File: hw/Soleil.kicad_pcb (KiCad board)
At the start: 2 copper layers, 31.4 x 44 mm, 54 parts, among them J1 Conn_01x04, Q1 MMBT3904, Q2 Si2301, Q3 2N7002, SW1 SW_Push, U1 SPV1040TTR, U2 XS3A1T3157GMX, U3 TPS61220DCK, U4 STM32G030F6Px, U5 ZJY200200-0154DAAMFGN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

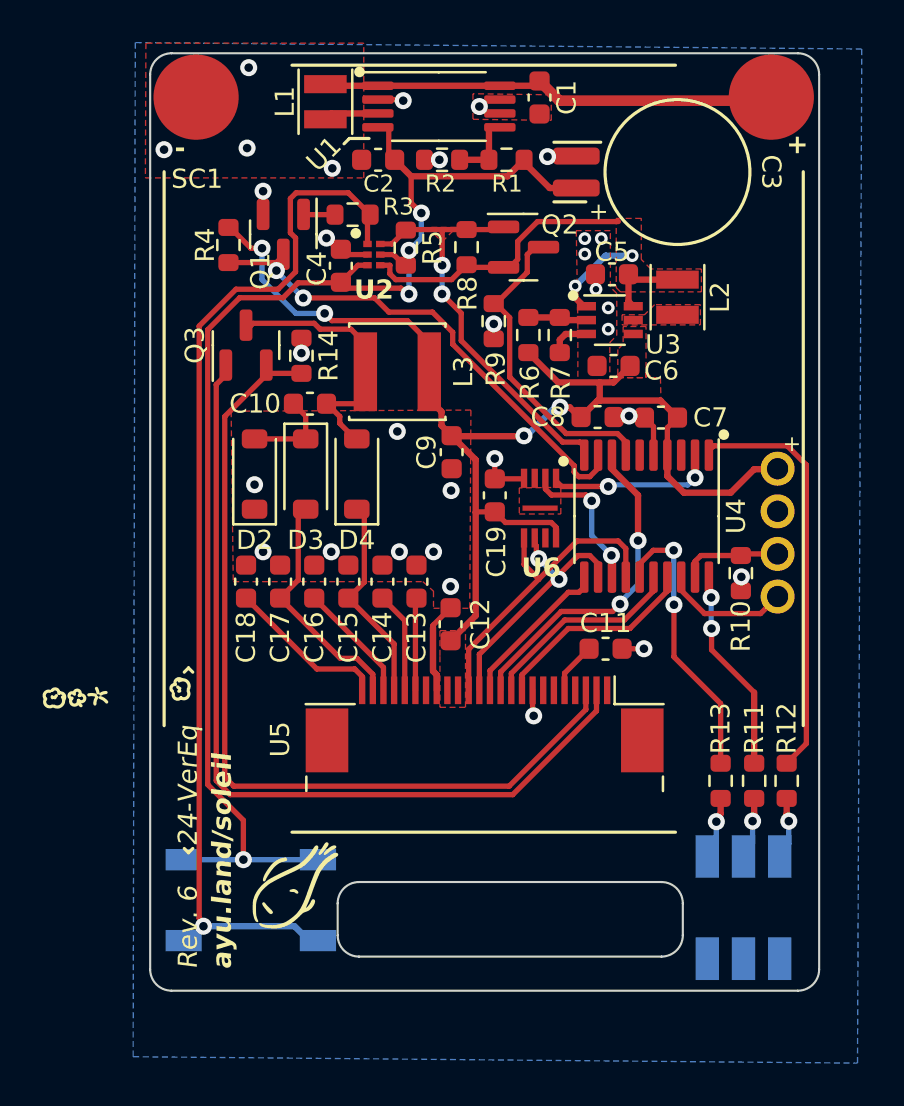
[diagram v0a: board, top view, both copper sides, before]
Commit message: Revise hardware and submit for fabrication (Rev. 6)
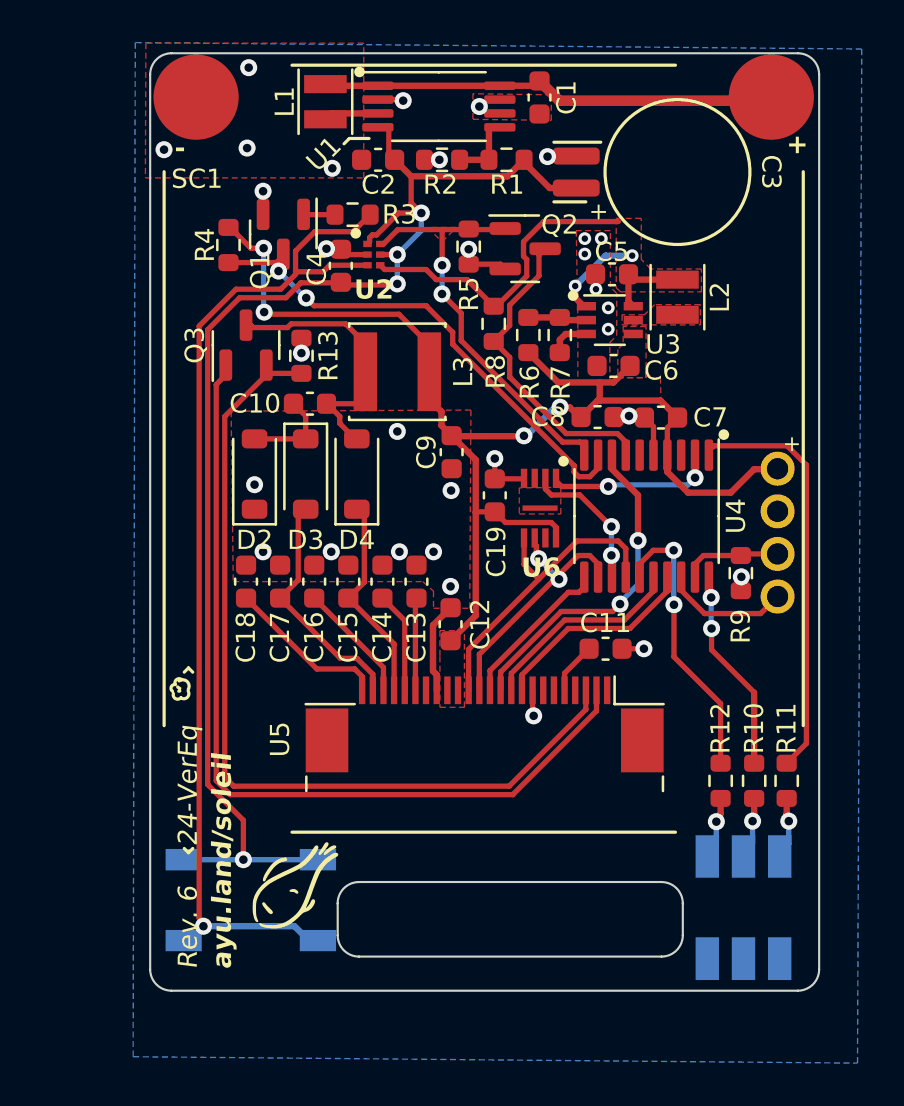
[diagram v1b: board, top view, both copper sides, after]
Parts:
- removed the R8 at (20.9, 18.5)
- Q2: value Si2301 -> 2N7002
- moved R5 2.95 mm to (21.1, 18.5), turned to -90 degrees
- moved R8 0.12 mm to (22.2, 22.1)
- moved Q2 0.11 mm to (23.7, 18.6)
- renumbered R11 to R10, R12 to R11, R13 to R12, R14 to R13, R9 to R8, R10 to R9
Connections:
- Q2 pad 2: VRI -> GND
- R3 pad 2: Net-(U2-Y2) -> Net-(U2-Y1)
- R5 pad 1: VCAP -> PWR_LATCH
- R5 pad 2: PWR_LATCH -> GND
- R8 pad 1: VRI_SENSE -> VRI
- R8 pad 2: GND -> VRI_SENSE
- SW1 pad 2: Net-(U2-Y2) -> Net-(U2-Y1)
- U2 pad 1: Net-(U2-Y2) -> VCAP
- U2 pad 3: VCAP -> Net-(U2-Y1)
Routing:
- net Net-(U2-Y2): track 49.6 -> 0.00 mm, vias 1 -> 0
- net Net-(U2-Y1): track 0.00 -> 49.1 mm, vias 0 -> 1
- net GND: track 21.5 -> 23.1 mm
- net VRI: track 21.9 -> 23.3 mm
- net VDD: track 60.6 -> 61.3 mm
- net VCAP: track 64.1 -> 63.5 mm

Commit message: Update layout, 🚧 routing to-do
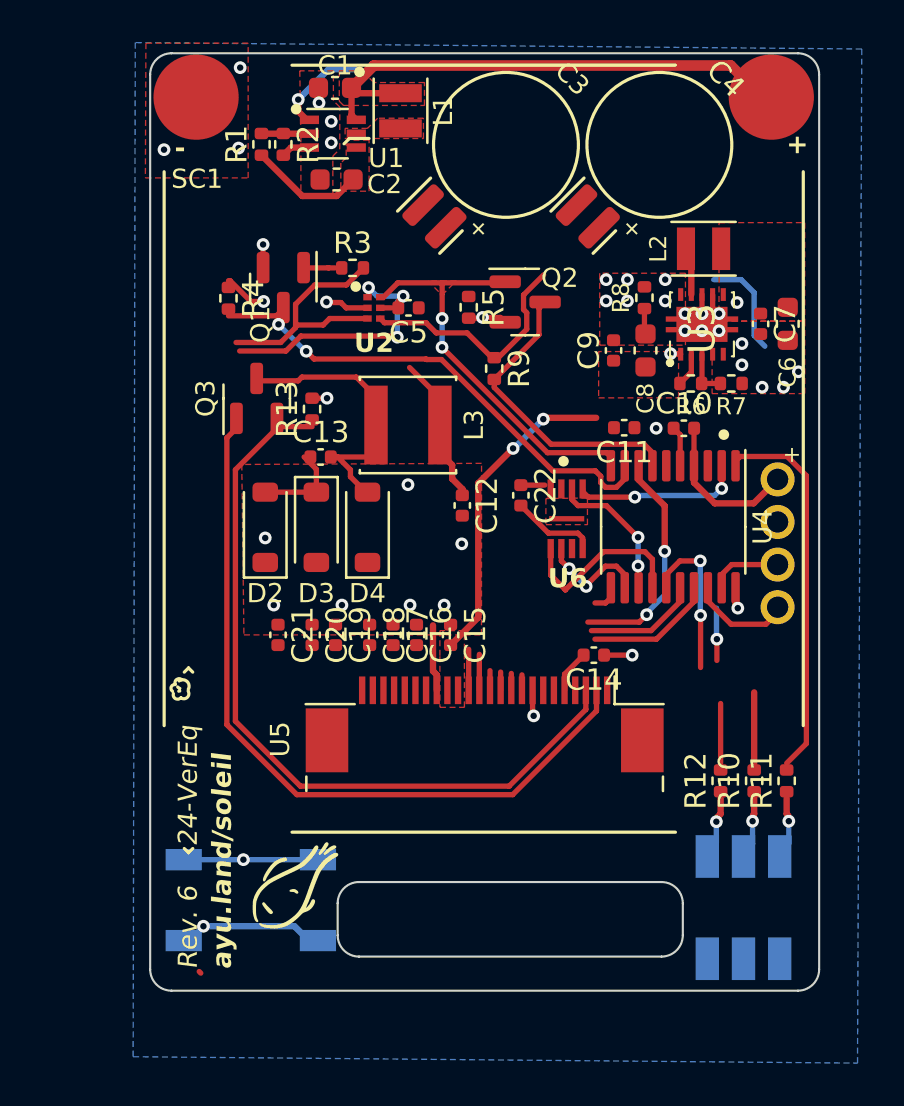
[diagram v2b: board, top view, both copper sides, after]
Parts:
- removed the C1 at (24.4, 11.5)
- removed the C2 at (16.8, 14.4)
- removed the L1 at (14.3, 11.7)
- removed the R1 at (22.8, 14.4)
- removed the R2 at (19.8, 14.4)
- removed the R9 at (33.8, 33.8)
- removed the U1 at (19.6, 11.9)
- added C4: 220m, Soleil_footprints:DMS3R3, F.Cu at (30.0, 13.7)
- added C6: 10u, Capacitor_SMD:C_0603_1608Metric, F.Cu at (36.0, 22.1)
- added C7: 100n, Capacitor_SMD:C_0402_1005Metric, F.Cu at (34.8, 22.1)
- added C8: 10u, Capacitor_SMD:C_0603_1608Metric, F.Cu at (29.4, 23.4)
- added C9: 2.2u, Capacitor_SMD:C_0402_1005Metric, F.Cu at (27.9, 23.4)
- added L2: 10u, Inductor_SMD:L_Sunlord_SWPA252012S, F.Cu at (32.1, 18.6)
- added R6: 560k, Resistor_SMD:R_0402_1005Metric, F.Cu at (31.5, 24.9)
- added R7: 100k, Resistor_SMD:R_0402_1005Metric, F.Cu at (33.4, 24.9)
- added R8: 1, Resistor_SMD:R_0402_1005Metric, F.Cu at (29.3, 20.9)
- added U3: TPS61020DRCR, Soleil_footprints:TPS61020DRCR, F.Cu at (32.0, 22.1)
- C10: renamed from C7; footprint Capacitor_SMD:C_0603_1608Metric -> Capacitor_SMD:C_0402_1005Metric
- C11: renamed from C8; footprint Capacitor_SMD:C_0603_1608Metric -> Capacitor_SMD:C_0402_1005Metric
- C12: renamed from C9; footprint Capacitor_SMD:C_0603_1608Metric -> Capacitor_SMD:C_0402_1005Metric
- C13: renamed from C10; footprint Capacitor_SMD:C_0603_1608Metric -> Capacitor_SMD:C_0402_1005Metric
- C14: renamed from C11; footprint Capacitor_SMD:C_0603_1608Metric -> Capacitor_SMD:C_0402_1005Metric
- C15: renamed from C12; footprint Capacitor_SMD:C_0603_1608Metric -> Capacitor_SMD:C_0402_1005Metric
- C16: renamed from C13; footprint Capacitor_SMD:C_0603_1608Metric -> Capacitor_SMD:C_0402_1005Metric
- C17: renamed from C14; footprint Capacitor_SMD:C_0603_1608Metric -> Capacitor_SMD:C_0402_1005Metric
- C18: renamed from C15; footprint Capacitor_SMD:C_0603_1608Metric -> Capacitor_SMD:C_0402_1005Metric
- C19: renamed from C16; footprint Capacitor_SMD:C_0603_1608Metric -> Capacitor_SMD:C_0402_1005Metric
- C20: renamed from C17; footprint Capacitor_SMD:C_0603_1608Metric -> Capacitor_SMD:C_0402_1005Metric
- C21: renamed from C18; footprint Capacitor_SMD:C_0603_1608Metric -> Capacitor_SMD:C_0402_1005Metric
- C22: renamed from C19; footprint Capacitor_SMD:C_0603_1608Metric -> Capacitor_SMD:C_0402_1005Metric
- C5: renamed from C4; footprint Capacitor_SMD:C_0603_1608Metric -> Capacitor_SMD:C_0402_1005Metric
- R1: renamed from R6; footprint Resistor_SMD:R_0603_1608Metric -> Resistor_SMD:R_0402_1005Metric
- R10, R11, R12, R13, R3, R4, R5: footprint Resistor_SMD:R_0603_1608Metric -> Resistor_SMD:R_0402_1005Metric
- R2: renamed from R7; footprint Resistor_SMD:R_0603_1608Metric -> Resistor_SMD:R_0402_1005Metric
- R9: renamed from R8; footprint Resistor_SMD:R_0603_1608Metric -> Resistor_SMD:R_0402_1005Metric
- moved R2 15.8 mm to (12.3, 13.7)
- moved C2 15.7 mm to (14.8, 15.3)
- moved L1 15.7 mm to (17.9, 12.1)
- moved U1 15.7 mm to (14.7, 13.2)
- moved C1 15.7 mm to (14.8, 11.0)
- moved R1 15.4 mm to (11.3, 13.7)
- moved C3 8.15 mm to (22.8, 13.7), turned to -135 degrees
- moved C5 3.74 mm to (18.2, 21.4), turned to 180 degrees
- moved C20 2.92 mm to (13.7, 36.7)
- moved C21 2.92 mm to (12.1, 36.7)
- moved R5 2.85 mm to (21.1, 21.3)
- moved C19 2.69 mm to (14.8, 36.7)
- moved C18 2.69 mm to (16.4, 36.7)
- moved C12 2.55 mm to (20.8, 30.6)
- moved C13 2.55 mm to (14.1, 28.4)
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- renumbered C5 to C1, C6 to C2, L2 to L1, U3 to U1
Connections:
- C1 pad 1: VRI -> Net-(SC1-+)
- C2 pad 1: VDD -> VCAP
- L1 pad 1: VRI -> Net-(SC1-+)
- R1 pad 1: VDD -> VCAP
- U1 pad 1: VRI -> Net-(SC1-+)
- U1 pad 4: VDD -> VCAP
- U1 pad 6: VRI -> Net-(SC1-+)
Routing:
- net VCAP: track 63.5 -> 24.9 mm
- net Net-(U2-Y1): track 49.1 -> 18.5 mm
- net VDD: track 61.3 -> 37.4 mm, vias 4 -> 3
- net VRI: track 23.3 -> 11.7 mm
- net EP_VGL: track 11.3 -> 0.00 mm
- net EP_VGH: track 9.92 -> 0.00 mm
- net Net-(U5-VCOM): track 7.62 -> 0.00 mm
- net Net-(SC1-+): track 21.7 -> 29.3 mm, vias 0 -> 1
- net Net-(U5-VSL): track 5.75 -> 0.00 mm
- net SPI_SCK: track 12.4 -> 6.96 mm
- net EP_CSN: track 7.44 -> 2.24 mm
- net EP_GDR: track 40.4 -> 35.4 mm
- net Net-(U5-VSH1): track 4.76 -> 0.00 mm
- net Net-(U5-VDD): track 4.70 -> 0.00 mm
- net SPI_MOSI: track 15.1 -> 10.5 mm
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- added copper zone on F.Cu, net Net-(SC1-+)
- added copper zone on F.Cu, net VCAP

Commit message: Finish board routing
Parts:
- C1, C2, C6, C8: footprint Capacitor_SMD:C_0603_1608Metric -> Capacitor_SMD:C_0402_1005Metric
- R3: value 470k -> 1M
- R4: value 470k -> 100k
- R6: value 560k -> 1M
- R7: value 100k -> 200k
- moved R3 0.74 mm to (15.1, 20.0), turned to -90 degrees
- moved R4 0.53 mm to (10.1, 21.3)
- moved C12 0.52 mm to (20.8, 30.1)
- moved C2 0.47 mm to (14.8, 14.8)
- moved R8 0.43 mm to (29.7, 20.9)
- moved C7 0.42 mm to (35.2, 22.1)
- moved C8 0.42 mm to (29.8, 23.4)
- moved C9 0.42 mm to (28.3, 23.4)
- moved L2 0.42 mm to (32.5, 18.6)
- moved R6 0.42 mm to (31.9, 24.9)
- moved R7 0.42 mm to (33.8, 24.9)
- moved U3 0.42 mm to (32.4, 22.1)
- moved C1 0.33 mm to (15.1, 10.9)
- moved C22 0.30 mm to (23.8, 30.1)
- moved L1 0.25 mm to (17.9, 11.8)
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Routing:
- net VCAP: track 24.9 -> 67.0 mm
- net Net-(U2-Y1): track 18.5 -> 44.6 mm
- net VRI: track 11.7 -> 35.5 mm
- net VDD: track 37.4 -> 56.9 mm, vias 3 -> 4
- net EP_VGL: track 0.00 -> 8.70 mm
- net EP_VGH: track 0.00 -> 6.96 mm
- net EP_CSN: track 2.24 -> 8.48 mm
- net SPI_SCK: track 6.96 -> 12.9 mm
- net EP_DCC: track 12.2 -> 17.3 mm
- net SPI_MOSI: track 10.5 -> 15.4 mm
- net Net-(U5-VCOM): track 0.00 -> 4.66 mm
- net EP_NRST: track 6.17 -> 10.8 mm
- net EP_BUSY: track 6.76 -> 10.9 mm
- net Net-(U5-VSL): track 0.00 -> 3.69 mm
- net Net-(U5-VSH1): track 0.00 -> 2.35 mm
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
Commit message: Finish board update; submit for fab (Rev. 7)
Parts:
- R1: value 560k -> 1M
- R2: value 100k -> 180k
- moved C10 0.29 mm to (31.2, 27.3)
- moved D1 0.20 mm to (34.0, 49.3)
- moved C9 0.15 mm to (28.4, 23.4)
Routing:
- net VRI: track 35.5 -> 34.3 mm
- net GND: track 23.6 -> 23.1 mm
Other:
- board text added: "24-Heat"
- board text added: "Rev. 7"
- board text removed: "24-VerEq"
- board text removed: "Rev. 6"
